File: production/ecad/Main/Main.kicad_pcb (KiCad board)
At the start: 2 copper layers, 59.5 x 82.5 mm, 12 parts, among them Q1 NMOS, Q2 NMOS, U1 TB6612FNG

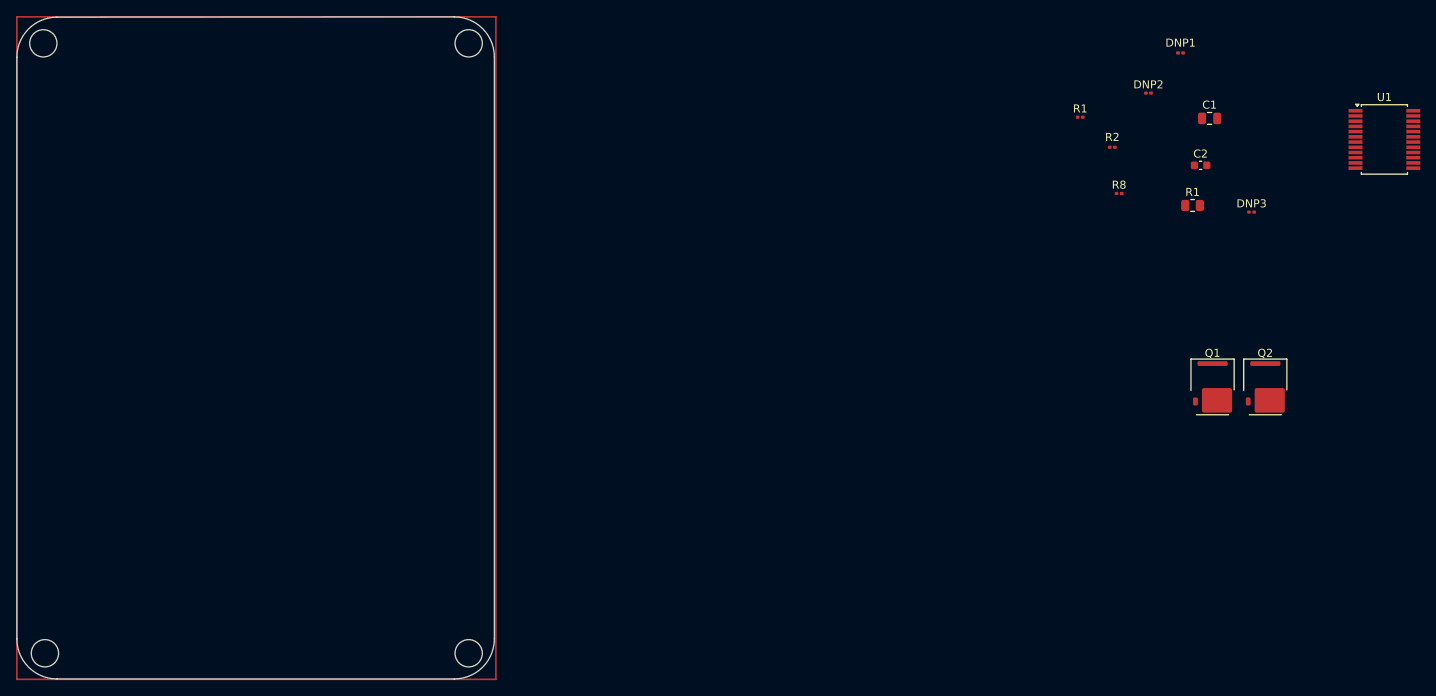
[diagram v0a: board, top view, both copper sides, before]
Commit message: Component placement complete
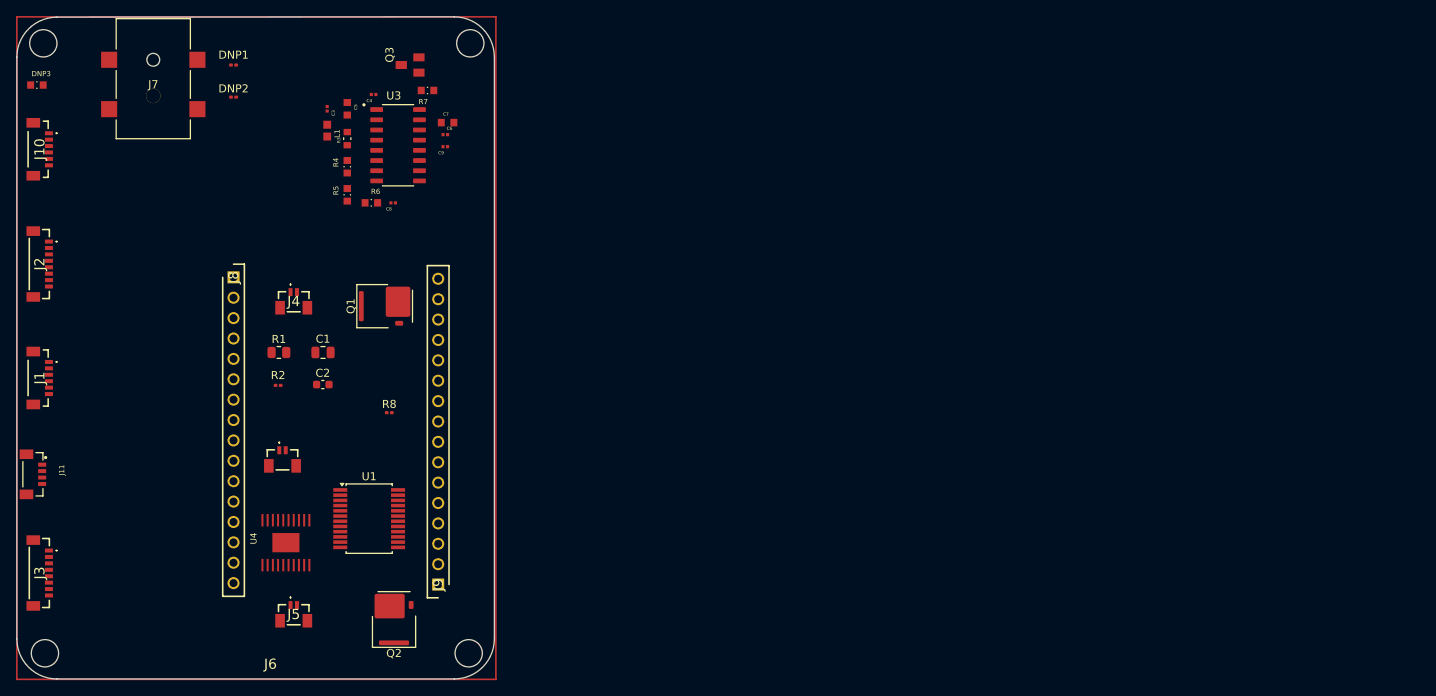
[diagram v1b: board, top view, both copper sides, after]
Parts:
- removed the R1 at (182.5, 62.0)
- added C3: 0.1uF, LoadCellFootprints:0p1uF, F.Cu at (88.7, 61.0)
- added C4: 0.1uF, LoadCellFootprints:0p1uF, F.Cu at (94.5, 59.2)
- added C5: 10uF, LoadCellFootprints:10uF, F.Cu at (91.2, 61.0)
- added C6: 0.1uF, LoadCellFootprints:0p1uF, F.Cu at (103.4, 64.2)
- added C7: 10uF, LoadCellFootprints:10uF, F.Cu at (103.7, 62.7)
- added C8: 0.1uF, LoadCellFootprints:0p1uF, F.Cu at (96.9, 72.7)
- added C9: 0.1uF, LoadCellFootprints:0p1uF, F.Cu at (103.4, 65.7)
- added J1: 214721-0061, Footprints:6_pos_connector, F.Cu at (52.7, 94.5)
- added J10: 214721-0061, LoadCellFootprints:6_pos_connector, F.Cu at (52.7, 66.0)
- added J11: 2147210040, Footprints:4positionheader, F.Cu at (52.0, 106.5)
- added J2: 214721-0100, Footprints:8positionheader, F.Cu at (52.8, 80.3)
- added J3: 214721-0080, Footprints:8positionheader, F.Cu at (52.8, 118.8)
- added J4: 214721-0020, Footprints:2positionheader, F.Cu at (84.5, 85.0)
- added J5: 214721-0020, Footprints:2positionheader, F.Cu at (84.5, 124.0)
- added J6: 214721-0020, Footprints:2positionheader, F.Cu at (83.1, 104.7)
- added J7: ADC-028-1-T/R-PA10T, Footprints:ADC-028-x-T&slash_R-PA10T_ADM, F.Cu at (67.0, 57.2)
- added J8: 61301611821, Footprints:15posheader, F.Cu at (77.0, 82.0)
- added J9: 61301611821, Footprints:15posheader, F.Cu at (102.5, 120.2)
- added L1: 3.3uH, LoadCellFootprints:inductor, F.Cu at (88.7, 63.7)
- added Q3: MMBT4403, LoadCellFootprints:mmbt4403, F.Cu at (99.0, 55.5)
- added R3: 20k, LoadCellFootprints:20k, F.Cu at (91.2, 64.7)
- added R4: 8.2K, LoadCellFootprints:8p2k, F.Cu at (91.2, 68.2)
- added R5: 100, LoadCellFootprints:100ohm, F.Cu at (91.2, 71.7)
- added R6: 100, LoadCellFootprints:100ohm, F.Cu at (94.2, 72.7)
- added R7: 10K, LoadCellFootprints:10k, F.Cu at (101.2, 58.7)
- added U3: HX711, LoadCellFootprints:HX711, F.Cu at (97.5, 65.5)
- added U4: TPS75233QPWPREP, Footprints:TPS75233QPWPREP, F.Cu at (83.5, 115.0)
- DNP3: footprint Resistor_SMD:R_0201_0603Metric -> LoadCellFootprints:10k
- moved DNP3 152.2 mm to (52.5, 58.0)
- moved U1 135.0 mm to (93.9, 112.0)
- moved DNP1 118.0 mm to (77.0, 55.5)
- moved R1 115.3 mm to (82.7, 91.3)
- moved C1 114.3 mm to (88.2, 91.3)
- moved DNP2 114.0 mm to (77.0, 59.5)
- moved C2 112.7 mm to (88.1, 95.3)
- moved Q2 112.4 mm to (97.0, 124.6), turned to 180 degrees
- moved R2 108.1 mm to (82.6, 95.4)
- moved Q1 103.6 mm to (95.8, 85.5), turned to 90 degrees
- moved R8 95.0 mm to (96.4, 98.8)
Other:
- outline, holes or cut-outs redrawn
- copper layers 2 -> 4

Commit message: GND, 5V, and 3v3 planes added
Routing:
- added copper zone on In1.Cu, net 3V3EXT
- added copper zone on In1.Cu, net 5VEXT
- added copper zone on In2.Cu, net GND
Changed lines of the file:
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@@
 		(tags "SSOP 0.65")
 		(property "Reference" "U1"
-			(at 0 -5.25 360)
+			(at 0 -5.25 0)
 			(layer "F.SilkS")
 			(effects
@@
 		)
 		(property "Value" "TB6612FNG"
-			(at 0 5.25 360)
+			(at 0 5.25 0)
 			(layer "F.Fab")
 			(effects
@@
 		)
 		(fp_text user "${REFERENCE}"
-			(at 0 0 360)
+			(at 0 0 0)
 			(layer "F.Fab")
 			(effects
@@
 		(tags "Connector")
 		(property "Reference" "J5"
-			(at 0 -0.05 360)
+			(at 0 -0.05 0)
 			(layer "F.SilkS")
 			(effects
@@
 		)
 		(property "Value" "214721-0020"
-			(at 0 -0.05 360)
+			(at 0 -0.05 0)
 			(layer "F.SilkS")
 			(hide yes)
@@
 		)
 		(fp_text user "${REFERENCE}"
-			(at 0 -0.05 360)
+			(at 0 -0.05 0)
 			(layer "F.Fab")
 			(effects
@@
 		(descr "<b>TO-236</b> ITT Intermetall")
 		(property "Reference" "Q3"
-			(at 1.271305 -2.542625 270)
+			(at 1.271305 -2.542625 -90)
 			(layer "F.SilkS")
 			(effects
@@
 		)
 		(property "Value" "MMBT4403"
-			(at 3.814945 2.543315 270)
+			(at 3.814945 2.543315 -90)
 			(layer "F.Fab")
 			(effects
@@
 		)
 		(property "Footprint" "LoadCellFootprints:mmbt4403"
-			(at 0 0 270)
+			(at 0 0 -90)
 			(layer "F.Fab")
 			(hide yes)
@@
 		)
 		(property "Datasheet" ""
-			(at 0 0 270)
+			(at 0 0 -90)
 			(layer "F.Fab")
 			(hide yes)
@@
 		)
 		(property "Description" ""
-			(at 0 0 270)
+			(at 0 0 -90)
 			(layer "F.Fab")
 			(hide yes)
@@
 		(at 91.17 68.175 90)
 		(property "Reference" "R4"
-			(at 0.532 -1.4064 270)
+			(at 0.532 -1.4064 -90)
 			(layer "F.SilkS")
 			(effects
@@
 		)
 		(property "Value" "8.2K"
-			(at 3.3768 1.3436 270)
+			(at 3.3768 1.3436 -90)
 			(layer "F.Fab")
 			(effects
@@
 		)
 		(property "Footprint" "LoadCellFootprints:8p2k"
-			(at 0 0 270)
+			(at 0 0 -90)
 			(layer "F.Fab")
 			(hide yes)
@@
 		)
 		(property "Datasheet" ""
-			(at 0 0 270)
+			(at 0 0 -90)
 			(layer "F.Fab")
 			(hide yes)
@@
 		)
 		(property "Description" ""
-			(at 0 0 270)
+			(at 0 0 -90)
 			(layer "F.Fab")
 			(hide yes)
@@
 		(tags "Connector")
 		(property "Reference" "J4"
-			(at 0 -0.05 360)
+			(at 0 -0.05 0)
 			(layer "F.SilkS")
 			(effects
@@
 		)
 		(property "Value" "214721-0020"
-			(at 0 -0.05 360)
+			(at 0 -0.05 0)
 			(layer "F.SilkS")
 			(hide yes)
@@
 		)
 		(fp_text user "${REFERENCE}"
-			(at 0 -0.05 360)
+			(at 0 -0.05 0)
 			(layer "F.Fab")
 			(effects
@@
 		(tags "ganpx gs66504b")
 		(property "Reference" "Q1"
-			(at 0 -4.21 270)
+			(at 0 -4.21 -90)
 			(layer "F.SilkS")
 			(effects
@@
 		)
 		(fp_text user "${REFERENCE}"
-			(at 0 0 360)
+			(at 0 0 0)
 			(layer "F.Fab")
 			(effects
@@
 		(at 83.5 115 90)
 		(property "Reference" "U4"
-			(at 0.5 -4 270)
+			(at 0.5 -4 -90)
 			(layer "F.SilkS")
 			(effects
@@
 		)
 		(property "Value" "TPS75233QPWPREP"
-			(at 0.5 -4 270)
+			(at 0.5 -4 -90)
 			(layer "F.Fab")
 			(effects
@@
 		(at 94.17 72.675)
 		(property "Reference" "R6"
-			(at 0.532 -1.4064 360)
+			(at 0.532 -1.4064 0)
 			(layer "F.SilkS")
 			(effects
@@
 		)
 		(property "Value" "100"
-			(at 3.3768 1.3436 360)
+			(at 3.3768 1.3436 0)
 			(layer "F.Fab")
 			(effects
@@
 		)
 		(property "Footprint" "LoadCellFootprints:100ohm"
-			(at 0 0 360)
+			(at 0 0 0)
 			(layer "F.Fab")
 			(hide yes)
@@
 		)
 		(property "Datasheet" ""
-			(at 0 0 360)
+			(at 0 0 0)
 			(layer "F.Fab")
 			(hide yes)
@@
 		)
 		(property "Description" ""
-			(at 0 0 360)
+			(at 0 0 0)
 			(layer "F.Fab")
 			(hide yes)
@@
 		(at 91.17 71.675 90)
 		(property "Reference" "R5"
-			(at 0.532 -1.4064 270)
+			(at 0.532 -1.4064 -90)
 			(layer "F.SilkS")
 			(effects
@@
 		)
 		(property "Value" "100"
-			(at 3.3768 1.3436 270)
+			(at 3.3768 1.3436 -90)
 			(layer "F.Fab")
 			(effects
@@
 		)
 		(property "Footprint" "LoadCellFootprints:100ohm"
-			(at 0 0 270)
+			(at 0 0 -90)
 			(layer "F.Fab")
 			(hide yes)
@@
 		)
 		(property "Datasheet" ""
-			(at 0 0 270)
+			(at 0 0 -90)
 			(layer "F.Fab")
 			(hide yes)
@@
 		)
 		(property "Description" ""
-			(at 0 0 270)
+			(at 0 0 -90)
 			(layer "F.Fab")
 			(hide yes)
@@
 		)
 		(fp_text user "${REFERENCE}"
-			(at 0 0 270)
+			(at 0 0 -90)
 			(layer "F.Fab")
 			(effects
@@
 		(tags "Connector")
 		(property "Reference" "J9"
-			(at 0 0 270)
+			(at 0 0 -90)
 			(layer "F.SilkS")
 			(effects
@@
 		)
 		(property "Value" "61301611821"
-			(at 0 0 270)
+			(at 0 0 -90)
 			(layer "F.SilkS")
 			(hide yes)
@@
 		)
 		(fp_text user "${REFERENCE}"
-			(at 0 0 270)
+			(at 0 0 -90)
 			(layer "F.Fab")
 			(effects
@@
 		(at 91.17 64.675 90)
 		(property "Reference" "R3"
-			(at -0.21 -1.05 270)
+			(at -0.21 -1.05 -90)
 			(layer "F.SilkS")
 			(effects
@@
 		)
 		(property "Value" "20k"
-			(at 1.54 1.05 270)
+			(at 1.54 1.05 -90)
 			(layer "F.Fab")
 			(effects
@@
 		)
 		(property "Footprint" "LoadCellFootprints:20k"
-			(at 0 0 270)
+			(at 0 0 -90)
 			(layer "F.Fab")
 			(hide yes)
@@
 		)
 		(property "Datasheet" ""
-			(at 0 0 270)
+			(at 0 0 -90)
 			(layer "F.Fab")
 			(hide yes)
@@
 		)
 		(property "Description" ""
-			(at 0 0 270)
+			(at 0 0 -90)
 			(layer "F.Fab")
 			(hide yes)
@@
 		(layer "Edge.Cuts")
 	)
+	(zone
+		(net 3)
+		(net_name "5VEXT")
+		(layer "In1.Cu")
+		(hatch edge 0.5)
+		(priority 1)
+		(connect_pads
+			(clearance 0.5)
+		)
+		(min_thickness 0.25)
+		(filled_areas_thickness no)
+		(fill
+			(thermal_gap 0.5)
+			(thermal_bridge_width 0.5)
+		)
+		(polygon
+			(pts
+				(xy 52 51.5) (xy 108 51.5) (xy 108 91.5) (xy 51.5 91.5)
+			)
+		)
+	)
+	(zone
+		(net 1)
+		(net_name "3V3EXT")
+		(layer "In1.Cu")
+		(hatch edge 0.5)
+		(priority 2)
+		(connect_pads
+			(clearance 0.5)
+		)
+		(min_thickness 0.25)
+		(filled_areas_thickness no)
+		(fill
+			(thermal_gap 0.5)
+			(thermal_bridge_width 0.5)
+		)
+		(polygon
+			(pts
+				(xy 51.5 91.5) (xy 108 91.5) (xy 108 130) (xy 51.5 130)
+			)
+		)
+	)
+	(zone
+		(net 2)
+		(net_name "GND")
+		(layer "In2.Cu")
+		(hatch edge 0.5)
+		(connect_pads
+			(clearance 0.5)
+		)
+		(min_thickness 0.25)
+		(filled_areas_thickness no)
+		(fill
+			(thermal_gap 0.5)
+			(thermal_bridge_width 0.5)
+		)
+		(polygon
+			(pts
+				(xy 52 51.5) (xy 108 51.5) (xy 108 130) (xy 51.5 130)
+			)
+		)
+	)
 )

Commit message: did some routing
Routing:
- net 5VEXT: track 0.00 -> 150.0 mm, vias 0 -> 14
- net GND: track 0.00 -> 133.7 mm, vias 0 -> 17
- net 3V3EXT: track 0.00 -> 106.4 mm, vias 0 -> 14
- net Net-(U3-RATE): track 0.00 -> 55.8 mm, vias 0 -> 4
- net /Load_Cell_and_Amplifier/A+: track 0.00 -> 49.5 mm, vias 0 -> 2
- net /Load_Cell_and_Amplifier/A-: track 0.00 -> 47.0 mm, vias 0 -> 2
- net /Load_Cell_and_Amplifier/AVDD: track 0.00 -> 37.8 mm
- net VBR_MTR_EN1: track 0.00 -> 32.1 mm, vias 0 -> 2
- net Net-(Q3-C): track 0.00 -> 17.3 mm, vias 0 -> 2
- net Net-(DNP1-Pad1): track 0.00 -> 16.5 mm
- net Net-(Q1-S): track 0.00 -> 13.5 mm
- net Net-(J6-Pad2): track 0.00 -> 12.0 mm, vias 0 -> 2
- net Net-(Q2-S): track 0.00 -> 11.6 mm
- net Net-(U3-INA-): track 0.00 -> 11.1 mm, vias 0 -> 2
- net Net-(Q3-B): track 0.00 -> 11.0 mm, vias 0 -> 2
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
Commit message: more routing
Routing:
- net W_DAT: track 0.00 -> 58.6 mm, vias 0 -> 4
- net ANO_COMA: track 0.00 -> 54.8 mm, vias 0 -> 2
- net W_SCK: track 0.00 -> 53.5 mm, vias 0 -> 4
- net GND: track 133.7 -> 183.2 mm, vias 17 -> 22
- net ANO_SW1: track 0.00 -> 48.7 mm, vias 0 -> 2
- net ANO_ENCB: track 0.00 -> 46.8 mm, vias 0 -> 2
- net ANO_ENCA: track 0.00 -> 45.3 mm, vias 0 -> 2
- net Net-(U4-RESET'_OR_PG): track 0.00 -> 34.4 mm, vias 0 -> 2
- net ANO_SW5: track 0.00 -> 32.6 mm, vias 0 -> 2
- net ANO_SW4: track 0.00 -> 31.0 mm, vias 0 -> 2
- net ANO_SW3: track 0.00 -> 29.1 mm, vias 0 -> 2
- net 5VEXT: track 150.0 -> 178.6 mm, vias 14 -> 17
- net ANO_SW2: track 0.00 -> 27.5 mm, vias 0 -> 2
- net SCL: track 0.00 -> 16.0 mm, vias 0 -> 2

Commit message: just some more routing
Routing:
- net SDA: track 0.00 -> 68.6 mm, vias 0 -> 6
- net SCL: track 16.0 -> 71.6 mm, vias 2 -> 4
- net IMU_VOUT: track 0.00 -> 38.1 mm, vias 0 -> 2
- net 5VEXT: track 178.6 -> 213.1 mm, vias 17 -> 19
- net Net-(J6-Pad1): track 0.00 -> 16.0 mm, vias 0 -> 2
- net Net-(J11-SHIELD-PadS1): track 0.00 -> 10.4 mm, vias 0 -> 2

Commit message: more changes
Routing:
- net LCD_DS: track 0.00 -> 80.4 mm, vias 0 -> 2
- net LCD_BL: track 0.00 -> 76.8 mm, vias 0 -> 4
- net LCD_RST: track 0.00 -> 71.9 mm, vias 0 -> 2
- net GND: track 183.2 -> 196.4 mm, vias 22 -> 23

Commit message: changes
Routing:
- net LCD_CLK: track 0.00 -> 67.1 mm, vias 0 -> 4
- net LCD_CS: track 0.00 -> 65.1 mm, vias 0 -> 2
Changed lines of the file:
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@@
+	)
+	(segment
+		(start 81.5 100)
+		(end 81.58 99.92)
+		(width 0.2)
+		(layer "F.Cu")
+		(net 27)
+	)
+	(segment
+		(start 54.17 118.57)
+		(end 74.34 118.57)
+		(width 0.2)
+		(layer "F.Cu")
+		(net 27)
+	)
+	(segment
+		(start 81.58 99.92)
+		(end 102.5 99.92)
+		(width 0.2)
+		(layer "F.Cu")
+		(net 27)
+	)
+	(segment
+		(start 81.473846 111)
+		(end 81.510217 110.963629)
+		(width 0.2)
+		(layer "F.Cu")
+		(net 27)
+	)
+	(segment
+		(start 74.34 118.57)
+		(end 74.5 118.41)
+		(width 0.2)
+		(layer "F.Cu")
+		(net 27)
+	)
+	(segment
+		(start 74.5 111)
+		(end 81.473846 111)
+		(width 0.2)
+		(layer "F.Cu")
+		(net 27)
+	)
+	(segment
+		(start 54 118.4)
+		(end 54.17 118.57)
+		(width 0.2)
+		(layer "F.Cu")
+		(net 27)
+	)
+	(via
+		(at 74.5 111)
+		(size 0.6)
+		(drill 0.3)
+		(layers "F.Cu" "B.Cu")
+		(net 27)
+	)
+	(via
+		(at 81.5 100)
+		(size 0.6)
+		(drill 0.3)
+		(layers "F.Cu" "B.Cu")
+		(net 27)
+	)
+	(via
+		(at 81.510217 110.963629)
+		(size 0.6)
+		(drill 0.3)
+		(layers "F.Cu" "B.Cu")
+		(net 27)
+	)
+	(via
+		(at 74.5 118.41)
+		(size 0.6)
+		(drill 0.3)
+		(layers "F.Cu" "B.Cu")
+		(net 27)
+	)
+	(segment
+		(start 74.5 118.41)
+		(end 74.5 111)
+		(width 0.2)
+		(layer "B.Cu")
+		(net 27)
+	)
+	(segment
+		(start 81.510217 100.010217)
+		(end 81.5 100)
+		(width 0.2)
+		(layer "B.Cu")
+		(net 27)
+	)
+	(segment
+		(start 81.510217 110.963629)
+		(end 81.510217 100.010217)
+		(width 0.2)
+		(layer "B.Cu")
+		(net 27)
+	)
+	(segment
+		(start 80 102.5)
+		(end 80.04 102.46)
+		(width 0.2)
+		(layer "F.Cu")
+		(net 29)
+	)
+	(segment
+		(start 80.04 102.46)
+		(end 102.5 102.46)
+		(width 0.2)
+		(layer "F.Cu")
+		(net 29)
+	)
+	(segment
+		(start 78.965687 102.5)
+		(end 80 102.5)
+		(width 0.2)
+		(layer "F.Cu")
+		(net 29)
+	)
+	(segment
+		(start 78.955687 119.01)
+		(end 78.965687 119)
+		(width 0.2)
+		(layer "F.Cu")
+		(net 29)
+	)
+	(segment
+		(start 54 119.2)
+		(end 54.19 119.01)
+		(width 0.2)
+		(layer "F.Cu")
+		(net 29)
+	)
+	(segment
+		(start 54.19 119.01)
+		(end 78.955687 119.01)
+		(width 0.2)
+		(layer "F.Cu")
+		(net 29)
+	)
+	(via
+		(at 78.965687 119)
+		(size 0.6)
+		(drill 0.3)
+		(layers "F.Cu" "B.Cu")
+		(net 29)
+	)
+	(via
+		(at 78.965687 102.5)
+		(size 0.6)
+		(drill 0.3)
+		(layers "F.Cu" "B.Cu")
+		(net 29)
+	)
+	(segment
+		(start 78.965687 119)
+		(end 78.965687 102.5)
+		(width 0.2)
+		(layer "B.Cu")
+		(net 29)
 	)
 	(segment

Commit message: my final changes
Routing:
- net GND: track 196.4 -> 249.0 mm, vias 23 -> 24
- net 3V3EXT: track 106.4 -> 143.1 mm, vias 14 -> 16
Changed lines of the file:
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@@
+	)
+	(segment
+		(start 56.748529 115.9)
+		(end 56.878529 116.03)
+		(width 0.2)
+		(layer "F.Cu")
+		(net 1)
 	)
 	(segment
@@
 	)
 	(segment
+		(start 79.695687 116.03)
+		(end 80.165687 116.5)
+		(width 0.2)
+		(layer "F.Cu")
+		(net 1)
+	)
+	(segment
 		(start 85.8 117.82)
 		(end 84.5 117.82)
@@
 	)
 	(segment
+		(start 80.5 121)
+		(end 80.6 120.9)
+		(width 0.2)
+		(layer "F.Cu")
+		(net 1)
+	)
+	(segment
 		(start 88.5 90)
 		(end 87.5 90)
@@
 	)
 	(segment
+		(start 54 116)
+		(end 54.1 115.9)
+		(width 0.2)
+		(layer "F.Cu")
+		(net 1)
+	)
+	(segment
 		(start 97 127.5)
 		(end 94 127.5)
@@
 	)
 	(segment
+		(start 85.9 120.9)
+		(end 86 121)
+		(width 0.2)
+		(layer "F.Cu")
+		(net 1)
+	)
+	(segment
+		(start 54.1 115.9)
+		(end 56.748529 115.9)
+		(width 0.2)
+		(layer "F.Cu")
+		(net 1)
+	)
+	(segment
 		(start 102.5 122.5)
 		(end 102.5 120.24)
@@
 	)
 	(segment
+		(start 56.878529 116.03)
+		(end 79.695687 116.03)
+		(width 0.2)
+		(layer "F.Cu")
+		(net 1)
+	)
+	(segment
 		(start 85.8 118.8)
 		(end 86 119)
@@
 	)
 	(segment
+		(start 80.6 120.9)
+		(end 85.9 120.9)
+		(width 0.2)
+		(layer "F.Cu")
+		(net 1)
+	)
+	(segment
 		(start 80.5 95)
 		(end 81.815 95)
@@
 	)
 	(via
+		(at 80.5 121)
+		(size 0.6)
+		(drill 0.3)
+		(layers "F.Cu" "B.Cu")
+		(net 1)
+	)
+	(via
+		(at 80.165687 116.5)
+		(size 0.6)
+		(drill 0.3)
+		(layers "F.Cu" "B.Cu")
+		(net 1)
+	)
+	(via
 		(at 80.5 95)
 		(size 0.6)
@@
 	)
 	(segment
+		(start 80.165687 116.5)
+		(end 80.165687 120.665687)
+		(width 0.2)
+		(layer "B.Cu")
+		(net 1)
+	)
+	(segment
 		(start 88.5 85.5)
 		(end 88.5 90)
@@
 	)
 	(segment
+		(start 80.165687 120.665687)
+		(end 80.5 121)
+		(width 0.2)
+		(layer "B.Cu")
+		(net 1)
+	)
+	(segment
 		(start 86 119)
 		(end 86 121)
@@
 	)
 	(segment
+		(start 90.3 110.4)
+		(end 90.3 109.75)
+		(width 0.2)
+		(layer "F.Cu")
+		(net 2)
+	)
+	(segment
 		(start 83.5 122.2)
 		(end 84.1 122.8)
@@
 	)
 	(segment
+		(start 56.5 116.5)
+		(end 75.98 116.5)
+		(width 0.2)
+		(layer "F.Cu")
+		(net 2)
+	)
+	(segment
+		(start 80.6 112.22)
+		(end 80.6 113.195)
+		(width 0.2)
+		(layer "F.Cu")
+		(net 2)
+	)
+	(segment
 		(start 97.855 66.135)
 		(end 94.83 66.135)
@@
 	)
 	(segment
+		(start 90.3 110.4)
+		(end 91.375 110.4)
+		(width 0.2)
+		(layer "F.Cu")
+		(net 2)
+	)
+	(segment
 		(start 51.72 58)
 		(end 51.72 58.72)
@@
 	)
 	(segment
+		(start 82.775 113.295)
+		(end 82.55 113.07)
+		(width 0.2)
+		(layer "F.Cu")
+		(net 2)
+	)
+	(segment
 		(start 83.2 117.82)
 		(end 83.2 119.2)
@@
 	)
 	(segment
+		(start 86.35 113.295)
+		(end 82.775 113.295)
+		(width 0.2)
+		(layer "F.Cu")
+		(net 2)
+	)
+	(segment
 		(start 93.455 68.955)
 		(end 93.5 69)
@@
 	)
 	(segment
+		(start 88.9 110.4)
+		(end 88.5 110)
+		(width 0.2)
+		(layer "F.Cu")
+		(net 2)
+	)
+	(segment
 		(start 77.019999 59)
 		(end 77.32 59.300001)
@@
 	)
 	(segment
+		(start 86.45 112.22)
+		(end 86.45 113.195)
+		(width 0.2)
+		(layer "F.Cu")
+		(net 2)
+	)
+	(segment
 		(start 87 114.5)
 		(end 88.33 114.5)
@@
 	)
 	(segment
+		(start 82.55 112.95)
+		(end 82.55 112.22)
+		(width 0.2)
+		(layer "F.Cu")
+		(net 2)
+	)
+	(segment
 		(start 100.17 63.595)
 		(end 103.518 63.595)
@@
 	)
 	(segment
+		(start 92.65 111.675)
+		(end 92.65 112.35)
+		(width 0.2)
+		(layer "F.Cu")
+		(net 2)
+	)
+	(segment
 		(start 103.67 64.175)
 		(end 103.73 64.175)
@@
 	)
 	(segment
+		(start 80.905 113.5)
+		(end 82 113.5)
+		(width 0.2)
+		(layer "F.Cu")
+		(net 2)
+	)
+	(segment
 		(start 74.349999 54.849999)
 		(end 74.5 55)
@@
 	)
 	(segment
+		(start 82.55 113.07)
+		(end 82.55 112.22)
+		(width 0.2)
+		(layer "F.Cu")
+		(net 2)
+	)
+	(segment
 		(start 91.17 68.955)
 		(end 93.455 68.955)
@@
 	)
 	(segment
+		(start 90.3 110.4)
+		(end 88.9 110.4)
+		(width 0.2)
+		(layer "F.Cu")
+		(net 2)
+	)
+	(segment
 		(start 88.75 84.6)
 		(end 84.2 84.6)
@@
 	)
 	(segment
+		(start 91.375 110.4)
+		(end 92.65 111.675)
+		(width 0.2)
+		(layer "F.Cu")
+		(net 2)
+	)
+	(segment
 		(start 88.9 95.32)
 		(end 88.125 94.545)
@@
 	)
 	(segment
+		(start 86.45 113.195)
+		(end 86.35 113.295)
+		(width 0.2)
+		(layer "F.Cu")
+		(net 2)
+	)
+	(segment
 		(start 89.1 84.95)
 		(end 88.75 84.6)
@@
 	)
 	(segment
+		(start 75.98 116.5)
+		(end 77 117.52)
+		(width 0.2)
+		(layer "F.Cu")
+		(net 2)
+	)
+	(segment
 		(start 88.53 114.3)
 		(end 86.45 112.22)
@@
 	)
 	(segment
+		(start 82 113.5)
+		(end 82.55 112.95)
+		(width 0.2)
+		(layer "F.Cu")
+		(net 2)
+	)
+	(segment
+		(start 80.6 113.195)
+		(end 80.905 113.5)
+		(width 0.2)
+		(layer "F.Cu")
+		(net 2)
+	)
+	(segment
 		(start 83.75 94.545)
 		(end 82.875 95.42)
@@
 	)
 	(via
+		(at 88.5 110)
+		(size 0.6)
+		(drill 0.3)
+		(layers "F.Cu" "B.Cu")
+		(net 2)
+	)
+	(via
 		(at 89 94)
 		(size 0.6)
@@
 	)
 	(segment
+		(start 88.5 110)
+		(end 88.5 96.5)
+		(width 0.2)
+		(layer "B.Cu")
+		(net 2)
+	)
+	(segment
 		(start 89.1 93.9)
 		(end 89 94)
@@
 		(width 0.2)
 		(layer "B.Cu")
+		(net 2)
+	)
+	(segment
+		(start 88.5 96.5)
+		(end 90 95)
+		(width 0.2)
+		(layer "B.Cu")
